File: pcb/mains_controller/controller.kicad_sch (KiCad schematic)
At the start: 32 parts, among them J1 Conn_01x03, J2 Conn_01x03, J3 RELAY_CONN, J4 Remote_header, J5 PWR_IN, J6 MFRC_CONN, J7 Micro_SD_Card, J8 Conn_01x03, J9 Conn_01x03, Q1 MMBT3906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

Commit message: Start design for mains controller
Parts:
- removed J3: RELAY_CONN, TerminalBlock_MetzConnect:TerminalBlock_MetzConnect_Type059_RT06302HBWC_1x02_P3.50mm_Horizontal, symbol Connector_Generic:Conn_01x02
- removed J4: Remote_header, TerminalBlock_MetzConnect:TerminalBlock_MetzConnect_Type059_RT06304HBWC_1x04_P3.50mm_Horizontal, symbol Connector_Generic:Conn_01x04
- removed J5: PWR_IN, TerminalBlock_MetzConnect:TerminalBlock_MetzConnect_Type059_RT06302HBWC_1x02_P3.50mm_Horizontal, symbol Connector_Generic:Conn_01x02
- removed JP1: RELAY_VOLT_SELECT, Jumper:SolderJumper-3_P1.3mm_Open_Pad1.0x1.5mm, symbol Jumper:SolderJumper_3_Open
- removed JP2, JP3: Jumper_2_Open, Jumper:SolderJumper-2_P1.3mm_Open_Pad1.0x1.5mm, symbol Jumper:Jumper_2_Open
- removed Q1, Q2: MMBT3906, Package_TO_SOT_SMD:SOT-23, symbol Transistor_BJT:MMBT3906
- removed R1: 5R1, Resistor_SMD:R_1210_3225Metric_Pad1.30x2.65mm_HandSolder, symbol Device:R
- removed R2: 470R, Resistor_SMD:R_1210_3225Metric_Pad1.30x2.65mm_HandSolder, symbol Device:R
- removed R8: R10K, Resistor_SMD:R_1210_3225Metric_Pad1.30x2.65mm_HandSolder, symbol Device:R
- removed U1: ~, RS485_to_ttl:RS485_to_ttl, symbol RS485_to_ttl:RS485_to_ttl
- removed U2: ~, DC-DC:hw-1338, symbol dc_dc:HW-1338
- added F1: Fuse, symbol Device:Fuse
- added K1: Relay_DPDT, symbol Relay:Relay_DPDT
- added PS1: HLK-PM01, Converter_ACDC:Converter_ACDC_Hi-Link_HLK-PMxx, symbol Converter_ACDC:HLK-PM01
- added RV1: Varistor, symbol Device:Varistor
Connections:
- net RELAY+ is gone; now on net +5V: D1.1 (K)
- net +5V: now also K1.A1, PS1.4 (+Vout)
- net GND: now also PS1.3 (-Vout)
- net RELAY-: now also K1.A2
- new net: F1.2, PS1.1 (AC/L), RV1.1
- new net LINE: F1.1, K1.11
- new net NEUT: K1.21, PS1.2 (AC/N), RV1.2
- new net SW_LINE: K1.14
- new net SW_NEUT: K1.24
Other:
- note removed: "5V Input select"
- note removed: "R8 optional to use RELAY- like a GPIO to toggle another device"
- note removed: "Remote end power feed jumper"

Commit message: Production version (sent to JLC!)
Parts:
- removed J8, J9: Conn_01x03, Connector_JST:JST_XH_B3B-XH-A_1x03_P2.50mm_Vertical, symbol Connector_Generic:Conn_01x03
- removed K1: Relay_DPDT, symbol Relay:Relay_DPDT
- added F2: Fuse, Resistor_THT:R_Axial_DIN0204_L3.6mm_D1.6mm_P5.08mm_Horizontal, symbol Device:Fuse
- added J3: Conn_01x03, TerminalBlock_MetzConnect:TerminalBlock_MetzConnect_Type073_RT02603HBLU_1x03_P5.08mm_Horizontal, symbol Connector_Generic:Conn_01x03
- added J4: Conn_01x04_Pin, Connector_JST:JST_XH_B4B-XH-A_1x04_P2.50mm_Vertical, symbol Connector:Conn_01x04_Pin
- added J5, J8: Conn_01x02_Pin, Connector_JST:JST_XH_B2B-XH-A_1x02_P2.50mm_Vertical, symbol Connector:Conn_01x02_Pin
- added K2: Relay_SPDT, Relay_THT:Relay_SPDT_Omron_G2RL-1-E, symbol Relay:Relay_SPDT
- added R1, R2: 4k7, Resistor_SMD:R_1210_3225Metric_Pad1.30x2.65mm_HandSolder, symbol Device:R
- F1: footprint (none) -> Fuse:Fuseholder_Clip-5x20mm_Keystone_3517_Inline_P23.11x6.76mm_D1.70mm_Horizontal
- RV1: footprint (none) -> Varistor:RV_Disc_D7mm_W4.9mm_P5mm
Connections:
- net +3V3: now also J4.1 (Pin_1), R1.1, R2.1
- net +5V: now also K2.A1
- net ACCESS_DENIED: now also J5.1 (Pin_1)
- net ACCESS_GRANTED: now also J8.1 (Pin_1)
- net GND: now also J4.2 (Pin_2), J5.2 (Pin_2), J8.2 (Pin_2)
- net LINE: now also J3.1 (Pin_1), K2.11
- net NEUT: now also J3.2 (Pin_2)
- net RELAY-: now also K2.A2
- net SW_LINE: now also K2.14
- net at F1.2, RV1.1: now also F2.1; no longer PS1.1 (AC/L)
- net RS485_RX renamed I2C0_SCL
- net I2C0_SCL: now also J4.4 (Pin_4), R1.2
- net RS485_TX renamed I2C0_SDA
- net I2C0_SDA: now also J4.3 (Pin_3), R2.2
- new net: F2.2, PS1.1 (AC/L)
- new net Earth: J3.3 (Pin_3)

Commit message: Add digikey PNs
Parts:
- added J9: Conn_01x03, TerminalBlock_MetzConnect:TerminalBlock_MetzConnect_Type073_RT02603HBLU_1x03_P5.08mm_Horizontal, symbol Connector_Generic:Conn_01x03
- F1: Digikey PN (none) -> 36-3517-ND
- F2: value Fuse -> Thermal fuse
- J3: Digikey PN (none) -> 609-3937-ND
- K2: value Relay_SPDT -> G2RL-1-E-DC5; Digikey (none) -> Z2824-ND
- RV1: Digikey PN (none) -> 118-MOV-07D301KTR
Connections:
- net Earth: now also J9.3 (Pin_3)
- net NEUT: now also J9.2 (Pin_2)
- net SW_LINE: now also J9.1 (Pin_1)
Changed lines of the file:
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@@
 			)
 		)
-		(property "Value" "Relay_SPDT"
+		(property "Value" "G2RL-1-E-DC5"
 			(at 165.1 74.9299 0)
 			(effects
@@
 			)
 		)
-		(property "Datasheet" "~"
+		(property "Datasheet" "G2RL-1-E DC5"
 			(at 153.67 73.66 0)
 			(effects
@@
 			)
 		)
+		(property "Digikey" "Z2824-ND"
+			(at 153.67 73.66 0)
+			(effects
+				(font
+					(size 1.27 1.27)
+				)
+				(hide yes)
+			)
+		)
 		(pin "A2"
 		)
@@
 			)
 		)
-		(property "Value" "Fuse"
+		(property "Value" "Thermal fuse"
 			(at 163.83 29.21 90)
 			(effects
@@
 			)
 		)
-		(property "Description" "Fuse"
+		(property "Description" "SF70E 70'C thermal fuse"
 			(at 163.83 33.02 0)
 			(effects
@@
 			)
 		)
+		(property "Digikey PN" " 609-3937-ND"
+			(at 210.82 43.18 0)
+			(effects
+				(font
+					(size 1.27 1.27)
+				)
+				(hide yes)
+			)
+		)
 		(pin "1"
 		)
@@
 			)
 		)
+		(property "Digikey PN" "36-3517-ND"
+			(at 147.32 33.02 90)
+			(effects
+				(font
+					(size 1.27 1.27)
+				)
+				(hide yes)
+			)
+		)
 		(pin "2"
 		)
@@
 	)
 	(symbol
+		(lib_id "Connector_Generic:Conn_01x03")
+		(at 210.82 66.04 0)
+		(unit 1)
+		(exclude_from_sim no)
+		(in_bom yes)
+		(on_board yes)
+		(dnp no)
+		(fields_autoplaced yes)
+		(property "Reference" "J9"
+			(at 213.36 64.7699 0)
+			(effects
+				(font
+					(size 1.27 1.27)
+				)
+				(justify left)
+			)
+		)
+		(property "Value" "Conn_01x03"
+			(at 213.36 67.3099 0)
+			(effects
+				(font
+					(size 1.27 1.27)
+				)
+				(justify left)
+			)
+		)
+		(property "Footprint" "TerminalBlock_MetzConnect:TerminalBlock_MetzConnect_Type073_RT02603HBLU_1x03_P5.08mm_Horizontal"
+			(at 210.82 66.04 0)
+			(effects
+				(font
+					(size 1.27 1.27)
+				)
+				(hide yes)
+			)
+		)
+		(property "Datasheet" "~"
+			(at 210.82 66.04 0)
+			(effects
+				(font
+					(size 1.27 1.27)
+				)
+				(hide yes)
+			)
+		)
+		(property "Description" "Generic connector, single row, 01x03, script generated (kicad-library-utils/schlib/autogen/connector/)"
+			(at 210.82 66.04 0)
+			(effects
+				(font
+					(size 1.27 1.27)
+				)
+				(hide yes)
+			)
+		)
+		(property "Digikey PN" ""
+			(at 210.82 66.04 0)
+			(effects
+				(font
+					(size 1.27 1.27)
+				)
+				(hide yes)
+			)
+		)
+		(property "Field6" "609-3937-ND"
+			(at 210.82 66.04 0)
+			(effects
+				(font
+					(size 1.27 1.27)
+				)
+				(hide yes)
+			)
+		)
+		(pin "1"
+		)
+		(pin "2"
+		)
+		(pin "3"
+		)
+		(instances
+			(project "controller"
+				(path "/c5633262-a594-4eb9-95d0-dd6b0b316893"
+					(reference "J9")
+					(unit 1)
+				)
+			)
+		)
+	)
+	(symbol
 		(lib_id "power:NEUT")
 		(at 200.66 66.04 0)
@@
 			(at 154.94 36.83 0)
 			(effects
+				(font
+					(size 1.27 1.27)
+				)
+				(hide yes)
+			)
+		)
+		(property "Digikey PN" "118-MOV-07D301KTR"
+			(at 154.94 36.83 0)
+			(effects

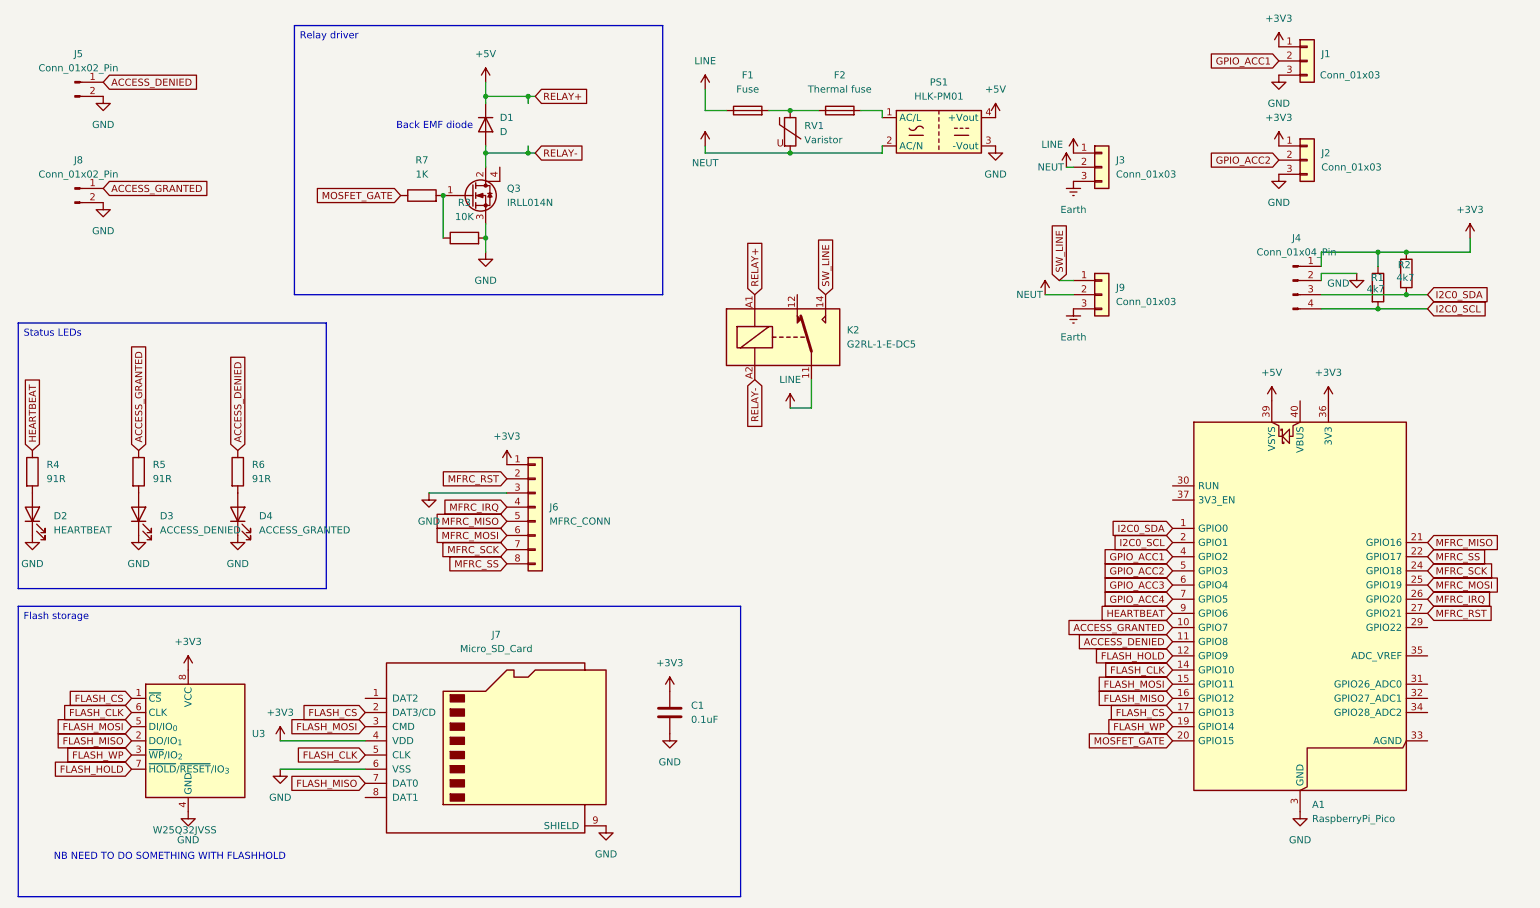
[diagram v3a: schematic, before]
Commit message: Fix LED labelling again
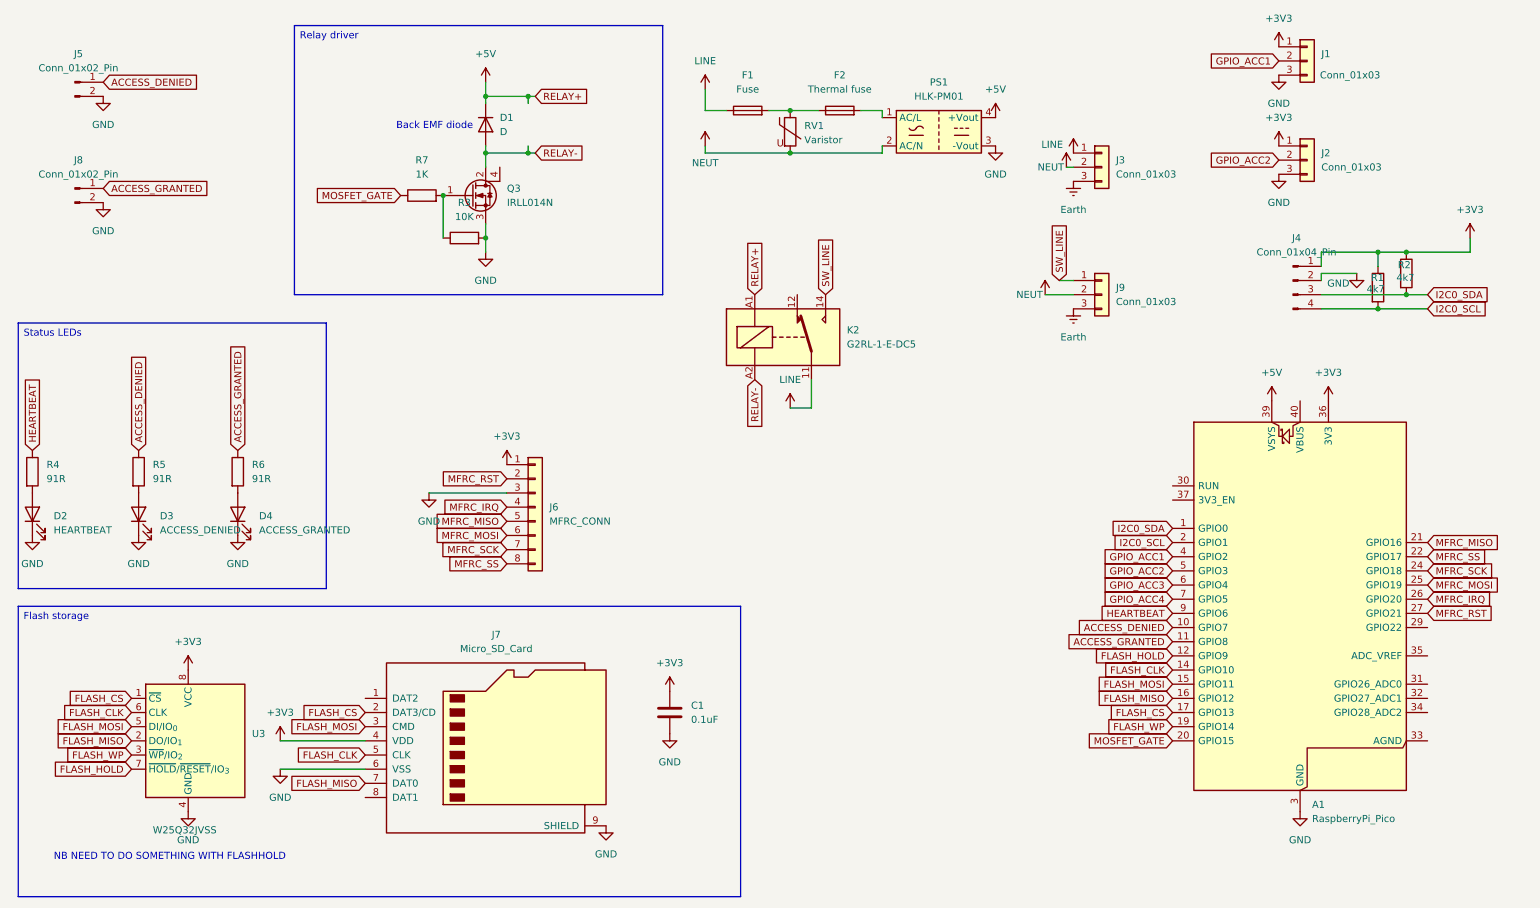
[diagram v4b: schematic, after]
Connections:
- net ACCESS_DENIED: now also A1.10 (GPIO7), R5.1; no longer A1.11 (GPIO8), R6.1
- net ACCESS_GRANTED: now also A1.11 (GPIO8), R6.1; no longer A1.10 (GPIO7), R5.1

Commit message: Fixes for pcb
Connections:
- net ACCESS_DENIED: now also J8.1 (Pin_1); no longer J5.1 (Pin_1)
- net ACCESS_GRANTED: now also J5.1 (Pin_1); no longer J8.1 (Pin_1)
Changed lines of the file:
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@@
 	(global_label "ACCESS_DENIED"
 		(shape input)
-		(at 31.75 27.94 0)
+		(at 31.75 46.99 0)
 		(fields_autoplaced yes)
 		(effects
@@
 		)
 		(property "Intersheetrefs" "${INTERSHEET_REFS}"
-			(at 49.6727 27.94 0)
+			(at 49.6727 46.99 0)
 			(effects
 				(font
@@
 	(global_label "ACCESS_GRANTED"
 		(shape input)
-		(at 31.75 46.99 0)
+		(at 31.75 27.94 0)
 		(fields_autoplaced yes)
 		(effects
@@
 		)
 		(property "Intersheetrefs" "${INTERSHEET_REFS}"
-			(at 51.2451 46.99 0)
+			(at 51.2451 27.94 0)
 			(effects
 				(font
